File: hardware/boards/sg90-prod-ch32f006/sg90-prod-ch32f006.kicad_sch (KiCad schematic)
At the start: 33 parts, among them J1 Servo Input, J2 Motor, J3 Debug, J4 Potentiometer, Q1 AO3401A, U1 TPAP2210K-3.3TRG1, U2 SN74LVC1G07DRLR_C19829624, U3 DRV8837DSGR-JSM, U4 CH32V006F8U6

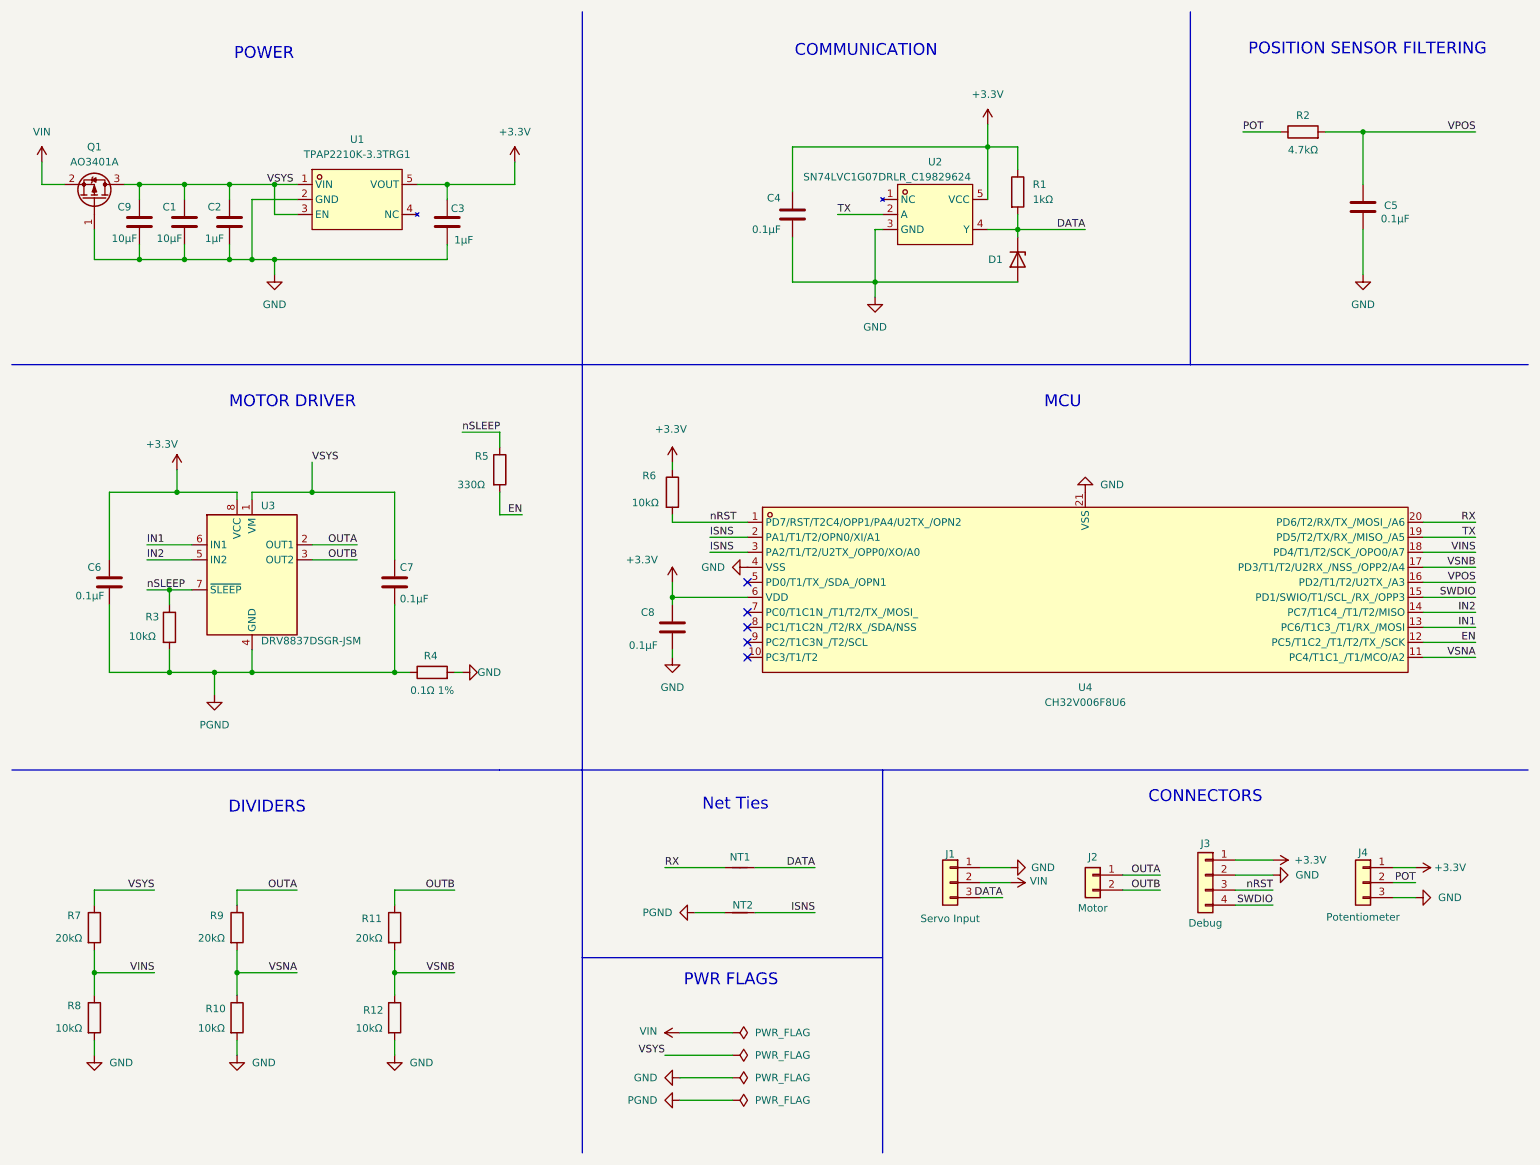
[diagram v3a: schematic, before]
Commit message: redid the PCB after finding a bunch of issues
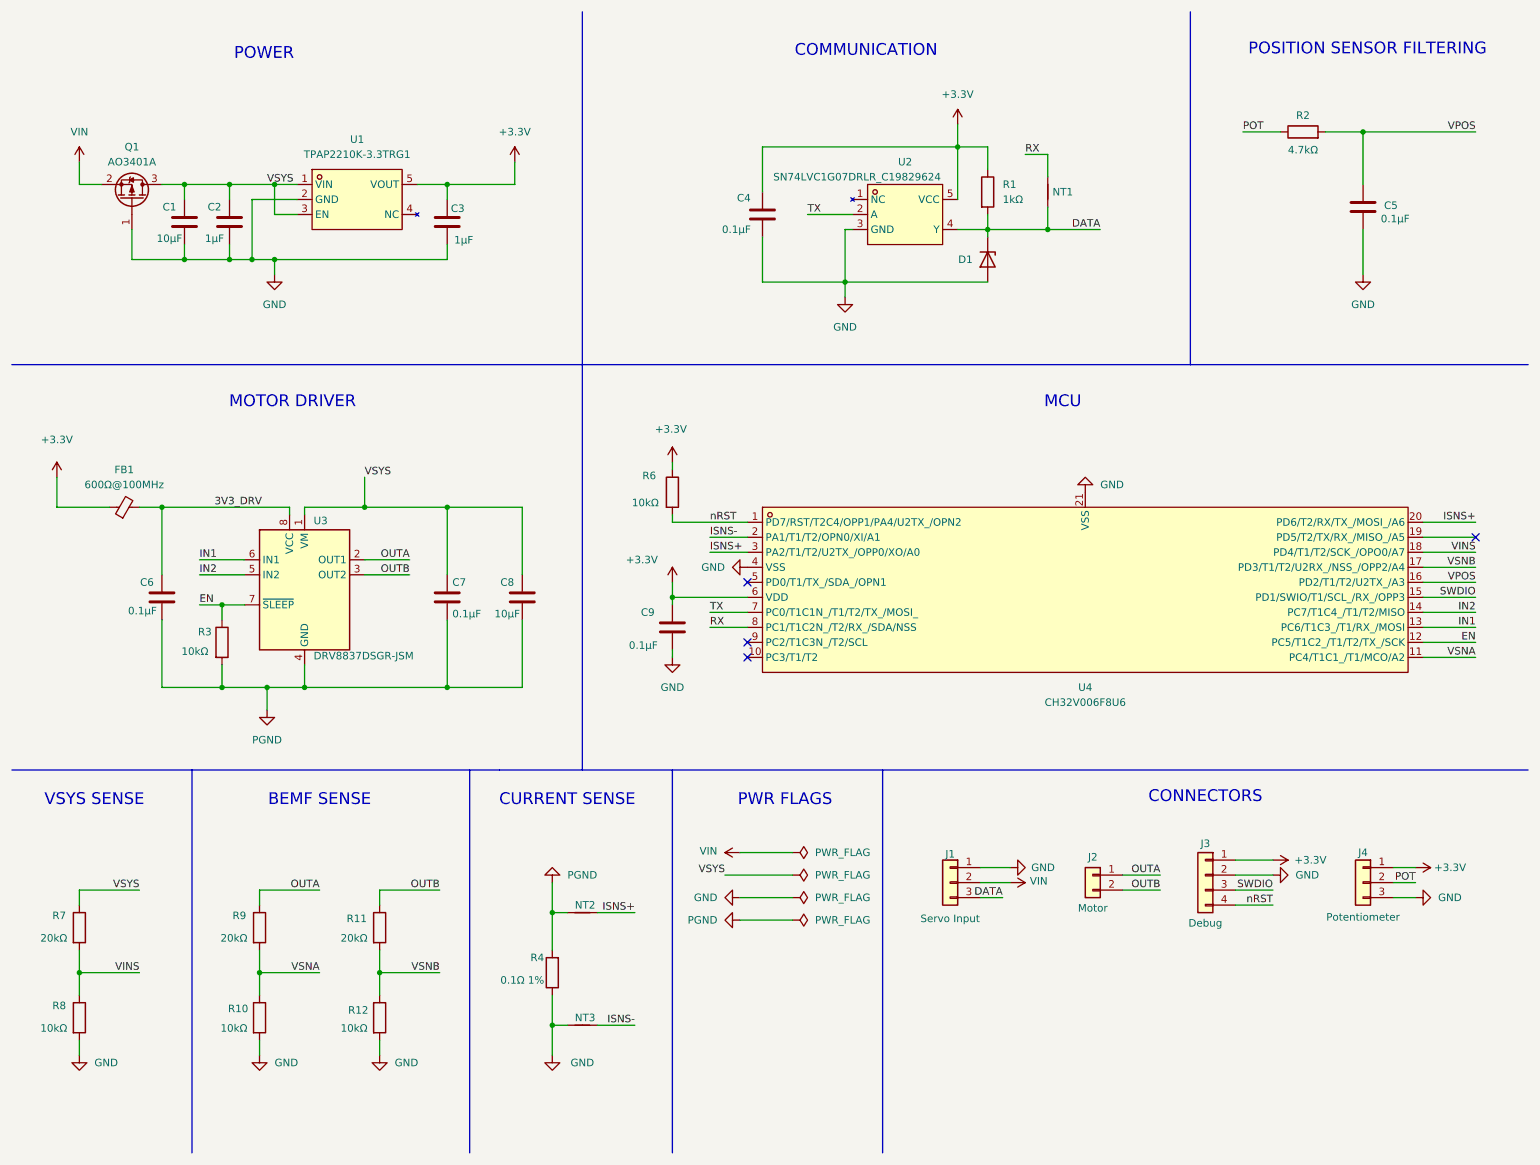
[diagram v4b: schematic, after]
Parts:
- removed R5: 330Ω, Resistor_SMD:R_0402_1005Metric, symbol Device:R
- added FB1: 600Ω@100MHz, Inductor_SMD:L_0603_1608Metric, symbol Device:FerriteBead_Small
- added NT3: NetTie_2, shared:NetTie-2_SMD_0.2mm, symbol Device:NetTie_2
- renumbered C9 to C8, C8 to C9
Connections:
- net nSLEEP is gone; now on net EN: R3.1, U3.7 (~{SLEEP})
- net +3.3V: now also FB1.1; no longer C6.1, U3.8 (VCC)
- net GND: now also R4.1, NT3.2; no longer C8.2, R4.2
- net PGND: now also C8.2, R4.2; no longer R4.1
- net RX: now also U4.8 (PC1/T1C2N_/T2/RX_/SDA/NSS); no longer U4.20 (PD6/T2/RX/TX_/MOSI_/A6)
- net SWDIO: now also J3.3 (Pin_3); no longer J3.4 (Pin_4)
- net TX: now also U4.7 (PC0/T1C1N_/T1/T2/TX_/MOSI_); no longer U4.19 (PD5/T2/TX/RX_/MISO_/A5)
- net nRST: now also J3.4 (Pin_4); no longer J3.3 (Pin_3)
- net ISNS renamed ISNS+
- net ISNS+: now also U4.20 (PD6/T2/RX/TX_/MOSI_/A6); no longer U4.2 (PA1/T1/T2/OPN0/XI/A1)
- new net 3V3_DRV: C6.1, FB1.2, U3.8 (VCC)
- new net ISNS-: NT3.1, U4.2 (PA1/T1/T2/OPN0/XI/A1)
- no-connect marks 5 -> 4
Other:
- note added: "BEMF SENSE"
- note added: "CURRENT SENSE"
- note added: "VSYS SENSE"
- note removed: "DIVIDERS"
- note removed: "Net Ties"
- moved on the sheet: C4, C6, C7, C8, D1, NT1, NT2, Q1, R1, R10, R11, R12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

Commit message: added NTC thermistor since CH32V006 doesn't have internal temp sensor
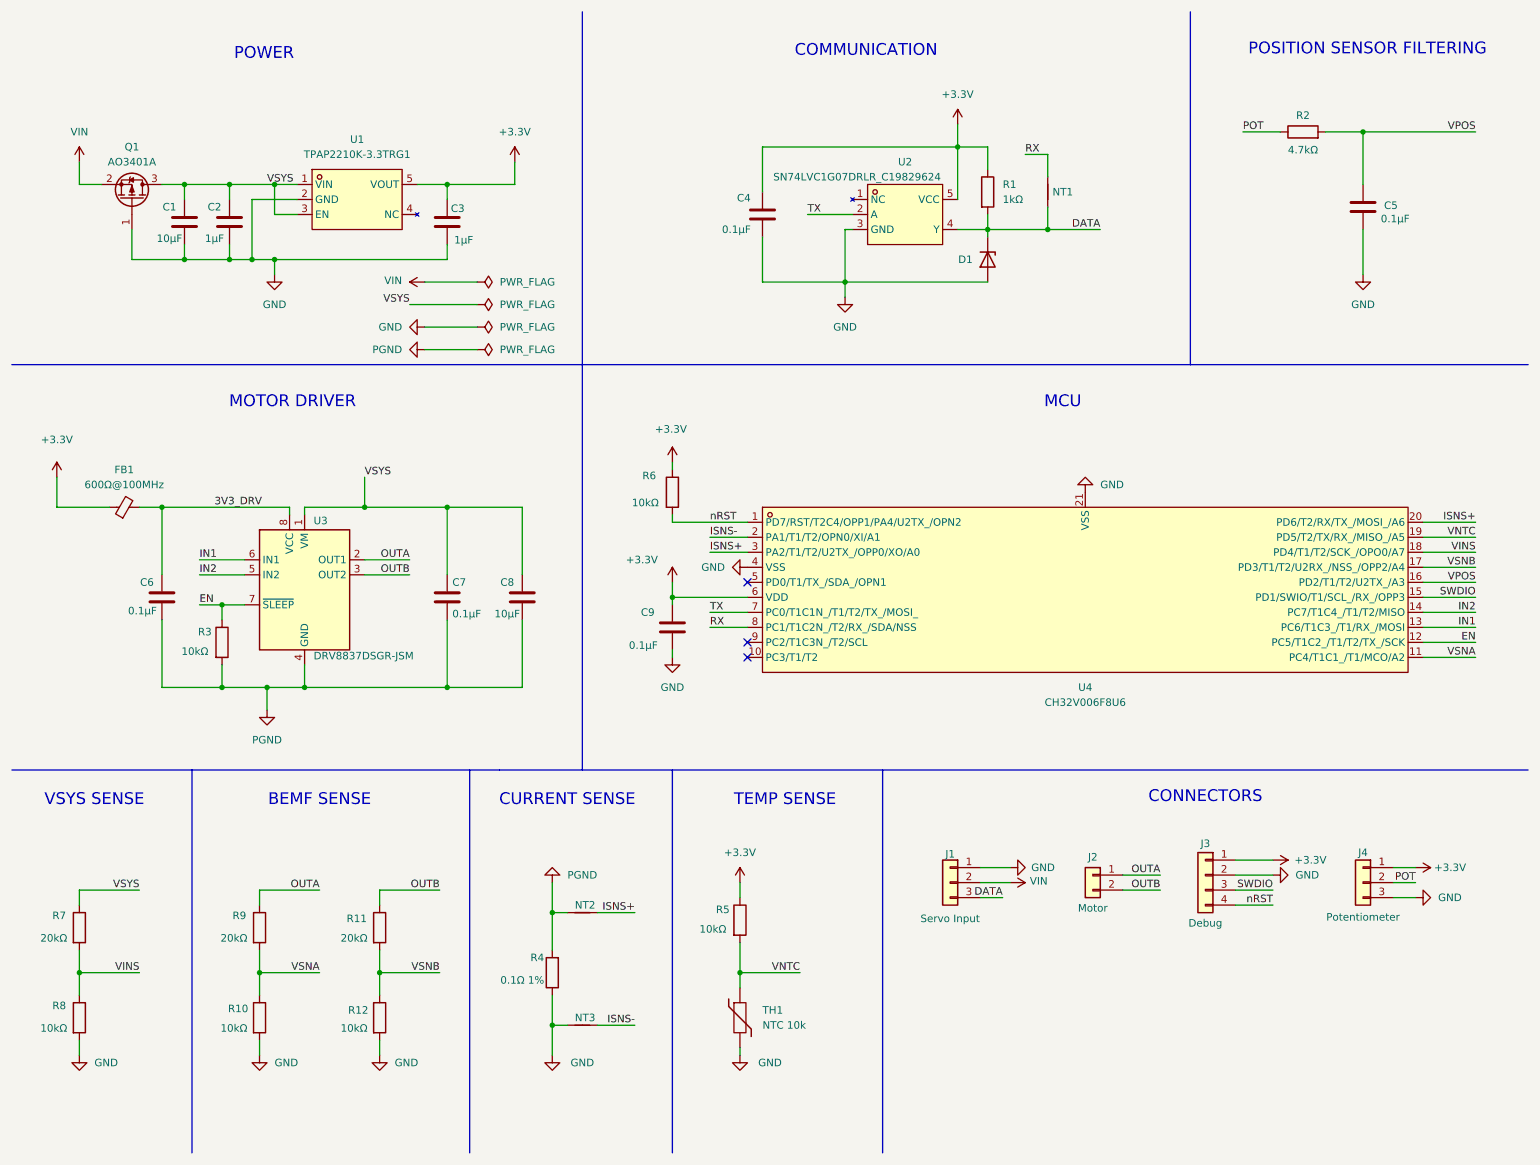
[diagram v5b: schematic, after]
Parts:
- added R5: 10kΩ, Resistor_SMD:R_0402_1005Metric, symbol Device:R
- added TH1: NTC 10k, Resistor_SMD:R_0402_1005Metric, symbol Device:Thermistor
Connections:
- net +3.3V: now also R5.1
- net GND: now also TH1.2
- net VNTC: now reaches U4.19 (PD5/T2/TX/RX_/MISO_/A5)
- net VNTC: now also R5.2, TH1.1
- no-connect marks 4 -> 3
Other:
- note added: "TEMP SENSE"
- note removed: "PWR FLAGS"
